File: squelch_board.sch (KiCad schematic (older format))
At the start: 84 parts, among them P1 PWR, P2 DISC., P3 OUT, P4 CONN_02X04, P5 CONN-10033526-N3212LF, P6 CONN_01X05, P7 LPF, P8 HPF, P9 DISC., U1 STM32F070F6P, U2 Ricom R-786.5-0.5, U3 AP2202, U4 MCP6002, U5 MCP6002, U6 CP2105

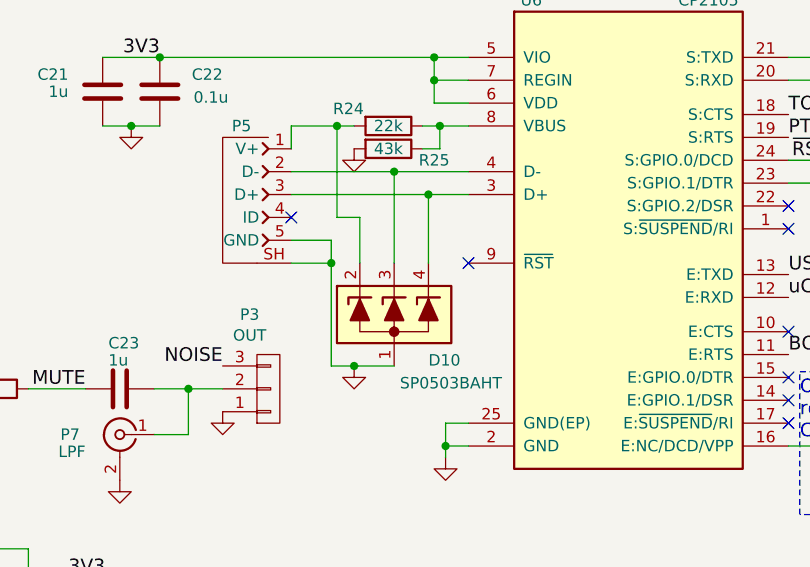
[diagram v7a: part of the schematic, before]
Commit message: Swapping out footprints for current ones in order to have 3d models
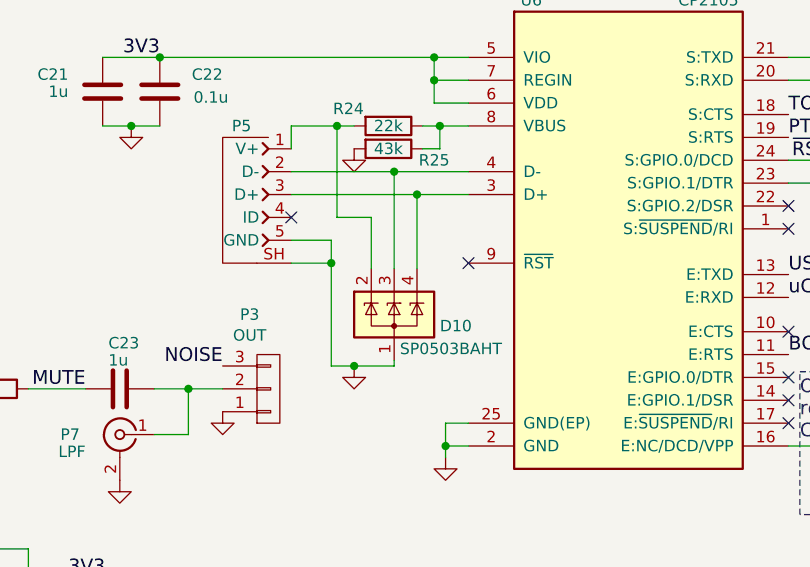
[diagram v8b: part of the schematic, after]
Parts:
- removed D10: SP0503BAHT, smd-semi:SOT-143, symbol squelch_board-rescue:SP0503BAHT
- added D10: SP0503BAHT, Package_TO_SOT_SMD:SOT-143, symbol Power_Protection:SP0503BAHT
- C1, C10, C14, C17, C18, C19, C2, C21, C22, C23, C25, C3, C4, C7, C9: footprint Capacitors_SMD:C_0603 -> Capacitor_SMD:C_0603_1608Metric
- C11, C13, C24, C5, C8: footprint Capacitors_SMD:C_0805 -> Capacitor_SMD:C_0805_2012Metric
- C6: footprint Capacitors_SMD:C_1206 -> Capacitor_SMD:C_1206_3216Metric
- D1, D2: footprint IPC7351-Nominal:DIOM5326X292 -> Diode_SMD:D_SMA
- D11, D12, D13: footprint LEDs:LED_0805 -> LED_SMD:LED_0805_2012Metric
- D4, D5, D6, D7, D8, D9: footprint LEDs:LED_0402 -> LED_SMD:LED_0402_1005Metric
- F1: footprint Resistors_SMD:R_1206 -> Resistor_SMD:R_1206_3216Metric
- FB1, FB2, R1, R10, R12, R13, R17, R19, R2, R20, R21, R24, R25, R26, R27, R28, R29, R3, R30, R31, R32, R33, R34, R4, R5, R6, R7, R8, R9: footprint Resistors_SMD:R_0603 -> Resistor_SMD:R_0603_1608Metric
- MP1, MP2, MP3, MP4: footprint MountingHole_3mm_Pad -> MountingHole:MountingHole_3mm_Pad
- P4: footprint Pin_Headers:Pin_Header_Angled_2x04_Pitch2.54mm -> Connector_PinHeader_2.54mm:PinHeader_2x04_P2.54mm_Horizontal
- P5: footprint conn-fci:CONN-10033526-N3212LF -> Connector_USB:USB_Mini-B_Lumberg_2486_01_Horizontal
- P6: footprint Pin_Headers:Pin_Header_Angled_1x05_Pitch2.54mm -> Connector_PinHeader_2.54mm:PinHeader_1x05_P2.54mm_Horizontal
- U3: footprint TO_SOT_Packages_SMD:SOT-23-5 -> Package_TO_SOT_SMD:SOT-23-5
- U4, U5: footprint Housings_SSOP:MSOP-8_3x3mm_Pitch0.65mm -> Package_SO:MSOP-8_3x3mm_P0.65mm
- U6: footprint IPC7351-Nominal:PQFN50P400X400X100-25 -> Package_DFN_QFN:QFN-24-1EP_4x4mm_P0.5mm_EP2.7x2.7mm
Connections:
- net GND: now also D10.1 (A)
- net at P5.3 (D+), U6.3 (D+): now also D10.4 (K)
- net at P5.2 (D-), U6.4 (D-): now also D10.3 (K)
- net at P5.1 (V+), R24.2: now also D10.2 (K)
